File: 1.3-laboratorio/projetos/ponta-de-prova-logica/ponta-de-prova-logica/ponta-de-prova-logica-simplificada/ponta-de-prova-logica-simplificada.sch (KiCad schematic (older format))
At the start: 19 parts

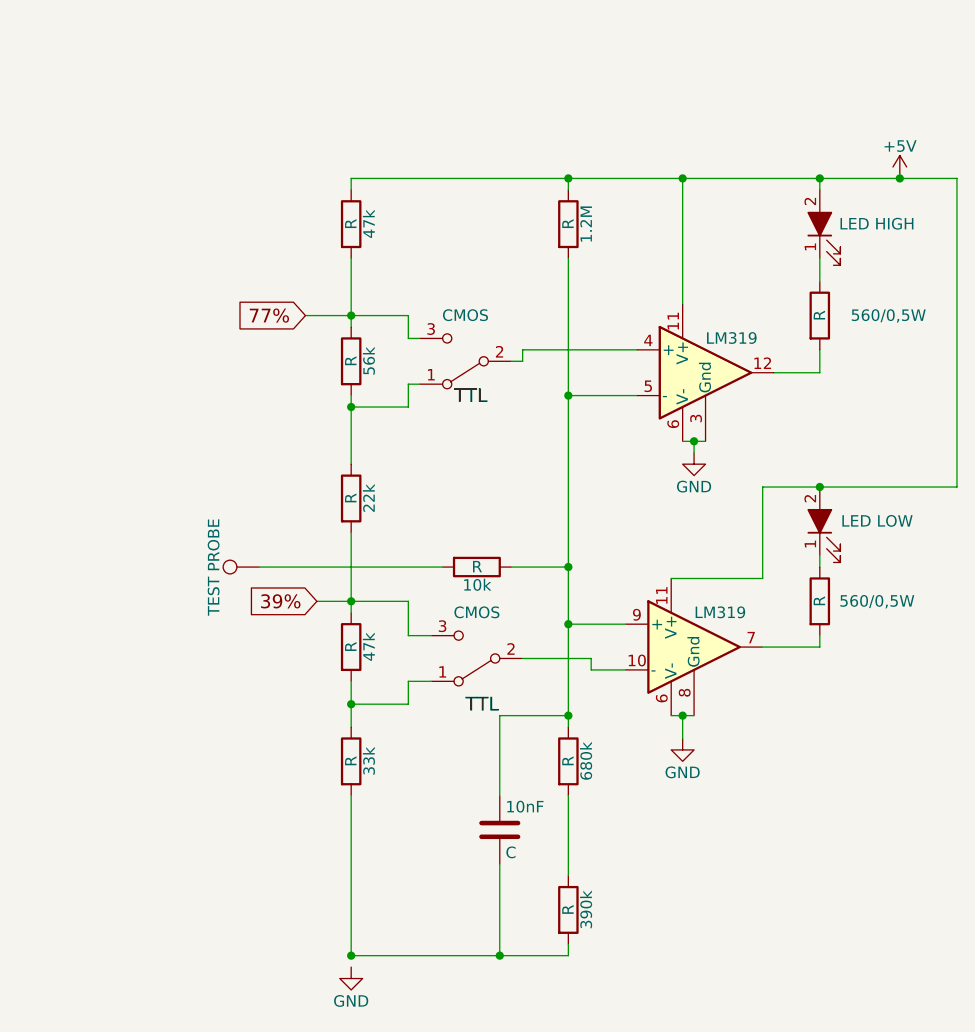
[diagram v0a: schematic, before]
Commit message: Desenho do Esquema PCB da ponta de prova lógica
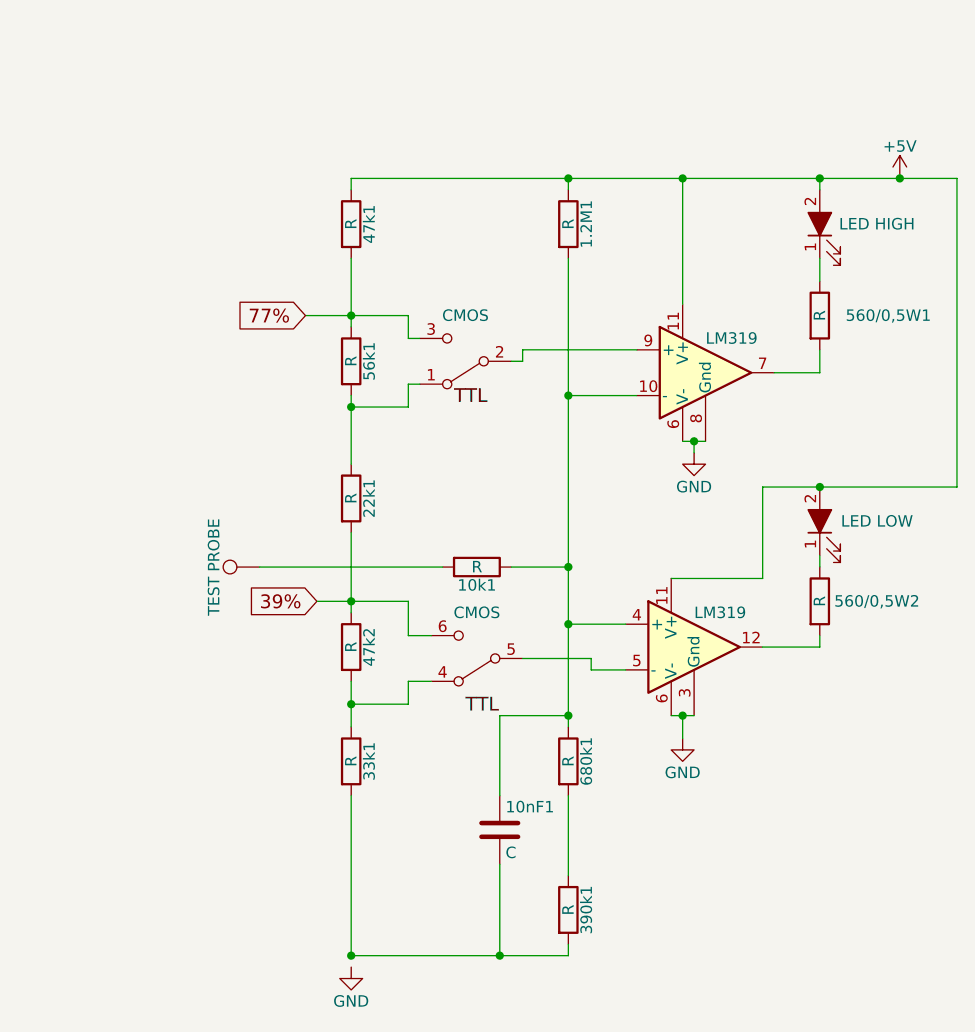
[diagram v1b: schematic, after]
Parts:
- 1.2M1: renamed from 1.2M; footprint (none) -> Resistors_THT:R_Axial_DIN0207_L6.3mm_D2.5mm_P7.62mm_Horizontal
- 10k1: renamed from 10k; footprint (none) -> Resistors_THT:R_Axial_DIN0207_L6.3mm_D2.5mm_P7.62mm_Horizontal
- 10nF1: renamed from 10nF; footprint (none) -> Capacitors_THT:C_Disc_D5.0mm_W2.5mm_P2.50mm
- 22k1: renamed from 22k; footprint (none) -> Resistors_THT:R_Axial_DIN0207_L6.3mm_D2.5mm_P7.62mm_Horizontal
- 33k1: renamed from 33k; footprint (none) -> Resistors_THT:R_Axial_DIN0207_L6.3mm_D2.5mm_P7.62mm_Horizontal
- 390k1: renamed from 390k; footprint (none) -> Resistors_THT:R_Axial_DIN0207_L6.3mm_D2.5mm_P7.62mm_Horizontal
- 47k1, 47k2: renamed from 47k; footprint (none) -> Resistors_THT:R_Axial_DIN0207_L6.3mm_D2.5mm_P7.62mm_Horizontal
- 560/0,5W1, 560/0,5W2: renamed from 560/0,5W; footprint (none) -> Resistors_THT:R_Axial_DIN0207_L6.3mm_D2.5mm_P7.62mm_Horizontal
- 56k1: renamed from 56k; footprint (none) -> Resistors_THT:R_Axial_DIN0207_L6.3mm_D2.5mm_P7.62mm_Horizontal
- 680k1: renamed from 680k; footprint (none) -> Resistors_THT:R_Axial_DIN0207_L6.3mm_D2.5mm_P7.62mm_Horizontal
- D1, D2: footprint (none) -> LEDs:LED_D1.8mm_W1.8mm_H2.4mm_Horizontal_O1.27mm_Z1.6mm
- J1: renamed from J?; footprint (none) -> Connectors:Pin_d1.0mm_L10.0mm
- TTL1: renamed from TTL; footprint (none) -> Buttons_Switches_THT:SW_CuK_JS202011AQN_DPDT_Angled
- U1: renamed from U?; footprint (none) -> Housings_DIP:DIP-14_W7.62mm
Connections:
- net 39%: now also TTL1.6 (C); no longer TTL1.3 (C)
- net GND: now also U1.3 (Gnd), U1.8 (Gnd); no longer U1.3 (Gnd), U1.8 (Gnd)
- net at 560/0,5W1.2: now also U1.7; no longer U1.12
- net at TTL1.2 (B): now also U1.9 (+); no longer U1.4 (+)
- net at 1.2M1.2, 10k1.1, 10nF1.1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: now also U1.10 (-), U1.4 (+); no longer U1.5 (-), U1.9 (+)
- net at 560/0,5W2.2: now also U1.12; no longer U1.7
- net at 33k1.1, 47k2.2: now also TTL1.4 (A); no longer TTL1.1 (A)
- new net: TTL1.5 (B), U1.5 (-)
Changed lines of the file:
@@
 LIBS:contrib
 LIBS:valves
+LIBS:ponta-de-prova-logica-simplificada-cache
 EELAYER 25 0
 EELAYER END
@@
 $EndDescr
 $Comp
-L LM319 U?
-U 1 1 5BBF01DE
+L LM319 U1
+U 2 1 5BBF01DE
 P 3850 2600
-F 0 "U?" H 3850 2850 50  0001 L CNN
+F 0 "U1" H 3850 2850 50  0001 L CNN
 F 1 "LM319" H 3850 2750 50  0000 L CNN
-F 2 "" H 3850 2600 50  0001 C CNN
+F 2 "Housings_DIP:DIP-14_W7.62mm" H 3850 2600 50  0001 C CNN
 F 3 "" H 3850 2600 50  0001 C CNN
-	1    3850 2600
-	1    0    0    -1
-$EndComp
-$Comp
-L +5V #PWR?
+	2    3850 2600
+	1    0    0    -1
+$EndComp
+$Comp
+L +5V #PWR01
 U 1 1 5BBF02C2
 P 4700 1750
-F 0 "#PWR?" H 4700 1600 50  0001 C CNN
+F 0 "#PWR01" H 4700 1600 50  0001 C CNN
 F 1 "+5V" H 4700 1890 50  0000 C CNN
 F 2 "" H 4700 1750 50  0001 C CNN
@@
 $EndComp
 $Comp
-L R 47k
+L R 47k2
 U 1 1 5BBF02DC
 P 2300 3800
-F 0 "47k" V 2380 3800 50  0000 C CNN
+F 0 "47k2" V 2380 3800 50  0000 C CNN
 F 1 "R" V 2300 3800 50  0000 C CNN
-F 2 "" V 2230 3800 50  0001 C CNN
+F 2 "Resistors_THT:R_Axial_DIN0207_L6.3mm_D2.5mm_P7.62mm_Horizontal" V 2230 3800 50  0001 C CNN
 F 3 "" H 2300 3800 50  0001 C CNN
 	1    2300 3800
@@
 $EndComp
 $Comp
-L R 33k
+L R 33k1
 U 1 1 5BBF0383
 P 2300 4300
-F 0 "33k" V 2380 4300 50  0000 C CNN
+F 0 "33k1" V 2380 4300 50  0000 C CNN
 F 1 "R" V 2300 4300 50  0000 C CNN
-F 2 "" V 2230 4300 50  0001 C CNN
+F 2 "Resistors_THT:R_Axial_DIN0207_L6.3mm_D2.5mm_P7.62mm_Horizontal" V 2230 4300 50  0001 C CNN
 F 3 "" H 2300 4300 50  0001 C CNN
 	1    2300 4300
@@
 $EndComp
 $Comp
-L R 56k
+L R 56k1
 U 1 1 5BBF0404
 P 2300 2550
-F 0 "56k" V 2380 2550 50  0000 C CNN
+F 0 "56k1" V 2380 2550 50  0000 C CNN
 F 1 "R" V 2300 2550 50  0000 C CNN
-F 2 "" V 2230 2550 50  0001 C CNN
+F 2 "Resistors_THT:R_Axial_DIN0207_L6.3mm_D2.5mm_P7.62mm_Horizontal" V 2230 2550 50  0001 C CNN
 F 3 "" H 2300 2550 50  0001 C CNN
 	1    2300 2550
@@
 $EndComp
 $Comp
-L R 22k
+L R 22k1
 U 1 1 5BBF043F
 P 2300 3150
-F 0 "22k" V 2380 3150 50  0000 C CNN
+F 0 "22k1" V 2380 3150 50  0000 C CNN
 F 1 "R" V 2300 3150 50  0000 C CNN
-F 2 "" V 2230 3150 50  0001 C CNN
+F 2 "Resistors_THT:R_Axial_DIN0207_L6.3mm_D2.5mm_P7.62mm_Horizontal" V 2230 3150 50  0001 C CNN
 F 3 "" H 2300 3150 50  0001 C CNN
 	1    2300 3150
@@
 $EndComp
 $Comp
-L R 390k
+L R 390k1
 U 1 1 5BBF0478
 P 3250 4950
-F 0 "390k" V 3330 4950 50  0000 C CNN
+F 0 "390k1" V 3330 4950 50  0000 C CNN
 F 1 "R" V 3250 4950 50  0000 C CNN
-F 2 "" V 3180 4950 50  0001 C CNN
+F 2 "Resistors_THT:R_Axial_DIN0207_L6.3mm_D2.5mm_P7.62mm_Horizontal" V 3180 4950 50  0001 C CNN
 F 3 "" H 3250 4950 50  0001 C CNN
 	1    3250 4950
@@
 $EndComp
 $Comp
-L R 680k
+L R 680k1
 U 1 1 5BBF04AF
 P 3250 4300
-F 0 "680k" V 3330 4300 50  0000 C CNN
+F 0 "680k1" V 3330 4300 50  0000 C CNN
 F 1 "R" V 3250 4300 50  0000 C CNN
-F 2 "" V 3180 4300 50  0001 C CNN
+F 2 "Resistors_THT:R_Axial_DIN0207_L6.3mm_D2.5mm_P7.62mm_Horizontal" V 3180 4300 50  0001 C CNN
 F 3 "" H 3250 4300 50  0001 C CNN
 	1    3250 4300
@@
 $EndComp
 $Comp
-L R 47k
+L R 47k1
 U 1 1 5BBF0ACE
 P 2300 1950
-F 0 "47k" V 2380 1950 50  0000 C CNN
+F 0 "47k1" V 2380 1950 50  0000 C CNN
 F 1 "R" V 2300 1950 50  0000 C CNN
-F 2 "" V 2230 1950 50  0001 C CNN
+F 2 "Resistors_THT:R_Axial_DIN0207_L6.3mm_D2.5mm_P7.62mm_Horizontal" V 2230 1950 50  0001 C CNN
 F 3 "" H 2300 1950 50  0001 C CNN
 	1    2300 1950
@@
 $EndComp
 $Comp
-L R 1.2M
+L R 1.2M1
 U 1 1 5BBF0B71
 P 3250 1950
-F 0 "1.2M" V 3330 1950 50  0000 C CNN
+F 0 "1.2M1" V 3330 1950 50  0000 C CNN
 F 1 "R" V 3250 1950 50  0000 C CNN
-F 2 "" V 3180 1950 50  0001 C CNN
+F 2 "Resistors_THT:R_Axial_DIN0207_L6.3mm_D2.5mm_P7.62mm_Horizontal" V 3180 1950 50  0001 C CNN
 F 3 "" H 3250 1950 50  0001 C CNN
 	1    3250 1950
@@
 $EndComp
 $Comp
-L R 560/0,5W
+L R 560/0,5W1
 U 1 1 5BBF0C0A
 P 4350 2350
-F 0 "560/0,5W" H 4650 2350 50  0000 C CNN
+F 0 "560/0,5W1" H 4650 2350 50  0000 C CNN
 F 1 "R" V 4350 2350 50  0000 C CNN
-F 2 "" V 4280 2350 50  0001 C CNN
+F 2 "Resistors_THT:R_Axial_DIN0207_L6.3mm_D2.5mm_P7.62mm_Horizontal" V 4280 2350 50  0001 C CNN
 F 3 "" H 4350 2350 50  0001 C CNN
 	1    4350 2350
@@
 $EndComp
 $Comp
-L R 10k
+L R 10k1
 U 1 1 5BBF0C7D
 P 2850 3450
-F 0 "10k" V 2930 3450 50  0000 C CNN
+F 0 "10k1" V 2930 3450 50  0000 C CNN
 F 1 "R" V 2850 3450 50  0000 C CNN
-F 2 "" V 2780 3450 50  0001 C CNN
+F 2 "Resistors_THT:R_Axial_DIN0207_L6.3mm_D2.5mm_P7.62mm_Horizontal" V 2780 3450 50  0001 C CNN
 F 3 "" H 2850 3450 50  0001 C CNN
 	1    2850 3450
@@
 F 0 "D1" H 4350 2050 50  0001 C CNN
 F 1 "LED HIGH" V 4350 1700 50  0000 C CNN
-F 2 "" H 4350 1950 50  0001 C CNN
+F 2 "LEDs:LED_D1.8mm_W1.8mm_H2.4mm_Horizontal_O1.27mm_Z1.6mm" H 4350 1950 50  0001 C CNN
 F 3 "" H 4350 1950 50  0001 C CNN
 	1    4350 1950
@@
 F 0 "D2" H 4350 3350 50  0001 C CNN
 F 1 "LED LOW" V 4350 3000 50  0000 C CNN
-F 2 "" H 4350 3250 50  0001 C CNN
+F 2 "LEDs:LED_D1.8mm_W1.8mm_H2.4mm_Horizontal_O1.27mm_Z1.6mm" H 4350 3250 50  0001 C CNN
 F 3 "" H 4350 3250 50  0001 C CNN
 	1    4350 3250
@@
 $EndComp
 $Comp
-L TEST_1P J?
+L TEST_1P J1
 U 1 1 5BBF1BCB
 P 1900 3450
-F 0 "J?" H 1900 3720 50  0001 C CNN
+F 0 "J1" H 1900 3720 50  0001 C CNN
 F 1 "TEST PROBE" H 1900 3650 50  0000 C CNN
-F 2 "" H 2100 3450 50  0001 C CNN
+F 2 "Connectors:Pin_d1.0mm_L10.0mm" H 2100 3450 50  0001 C CNN
 F 3 "" H 2100 3450 50  0001 C CNN
 	1    1900 3450
@@
 $EndComp
 $Comp
-L GND #PWR?
+L GND #PWR02
 U 1 1 5BBF1EC9
 P 2300 5200
-F 0 "#PWR?" H 2300 4950 50  0001 C CNN
+F 0 "#PWR02" H 2300 4950 50  0001 C CNN
 F 1 "GND" H 2300 5050 50  0000 C CNN
 F 2 "" H 2300 5200 50  0001 C CNN
@@
 $EndComp
 $Comp
-L R 560/0,5W
+L R 560/0,5W2
 U 1 1 5BBF372D
 P 4350 3600
-F 0 "560/0,5W" H 4600 3600 50  0000 C CNN
+F 0 "560/0,5W2" H 4600 3600 50  0000 C CNN
 F 1 "R" V 4350 3600 50  0000 C CNN
-F 2 "" V 4280 3600 50  0001 C CNN
+F 2 "Resistors_THT:R_Axial_DIN0207_L6.3mm_D2.5mm_P7.62mm_Horizontal" V 4280 3600 50  0001 C CNN
 F 3 "" H 4350 3600 50  0001 C CNN
 	1    4350 3600
@@
 $EndComp
 $Comp
-L GND #PWR?
+L GND #PWR03
 U 1 1 5BBF3B02
 P 3800 2950
-F 0 "#PWR?" H 3800 2700 50  0001 C CNN
+F 0 "#PWR03" H 3800 2700 50  0001 C CNN
 F 1 "GND" H 3800 2800 50  0000 C CNN
 F 2 "" H 3800 2950 50  0001 C CNN
@@
 $EndComp
 $Comp
-L GND #PWR?
+L GND #PWR04
 U 1 1 5BBF3BC6
 P 3750 4200
-F 0 "#PWR?" H 3750 3950 50  0001 C CNN
+F 0 "#PWR04" H 3750 3950 50  0001 C CNN
 F 1 "GND" H 3750 4050 50  0000 C CNN
 F 2 "" H 3750 4200 50  0001 C CNN
@@
 Connection ~ 4350 1750
 $Comp
-L SW_DPDT_x2 TTL
-U 1 1 5BBF4AF5
+L SW_DPDT_x2 TTL1
+U 2 1 5BBF4AF5
 P 2850 3850
-F 0 "TTL" H 2850 4020 50  0001 C CNN
+F 0 "TTL1" H 2850 4020 50  0001 C CNN
 F 1 "CMOS" H 2850 3650 50  0000 C CNN
-F 2 "" H 2850 3850 50  0001 C CNN
+F 2 "Buttons_Switches_THT:SW_CuK_JS202011AQN_DPDT_Angled" H 2850 3850 50  0001 C CNN
 F 3 "" H 2850 3850 50  0001 C CNN
-	1    2850 3850
+	2    2850 3850
 	-1   0    0    1
 $EndComp
@@
 Connection ~ 2300 4050
 $Comp
-L SW_DPDT_x2 TTL
+L SW_DPDT_x2 TTL1
 U 1 1 5BBF503E
 P 2800 2550
-F 0 "TTL" H 2800 2720 50  0001 C CNN
+F 0 "TTL1" H 2800 2720 50  0001 C CNN
 F 1 "CMOS" H 2800 2350 50  0000 C CNN
-F 2 "" H 2800 2550 50  0001 C CNN
+F 2 "Buttons_Switches_THT:SW_CuK_JS202011AQN_DPDT_Angled" H 2800 2550 50  0001 C CNN
 F 3 "" H 2800 2550 50  0001 C CNN
 	1    2800 2550
@@
 	4350 3800 4100 3800
 $Comp
-L LM319 U?
-U 2 1 5BBF0257
+L LM319 U1
+U 1 1 5BBF0257
 P 3800 3800
-F 0 "U?" H 3800 4050 50  0001 L CNN
+F 0 "U1" H 3800 4050 50  0001 L CNN
 F 1 "LM319" H 3800 3950 50  0000 L CNN
-F 2 "" H 3800 3800 50  0001 C CNN
+F 2 "Housings_DIP:DIP-14_W7.62mm" H 3800 3800 50  0001 C CNN
 F 3 "" H 3800 3800 50  0001 C CNN
-	2    3800 3800
+	1    3800 3800
 	1    0    0    -1
 $EndComp
@@
 77%
 $Comp
-L C 10nF
+L C 10nF1
 U 1 1 5BBF9380
 P 2950 4600
-F 0 "10nF" H 2975 4700 50  0000 L CNN
+F 0 "10nF1" H 2975 4700 50  0000 L CNN
 F 1 "C" H 2975 4500 50  0000 L CNN
-F 2 "" H 2988 4450 50  0001 C CNN
+F 2 "Capacitors_THT:C_Disc_D5.0mm_W2.5mm_P2.50mm" H 2988 4450 50  0001 C CNN
 F 3 "" H 2950 4600 50  0001 C CNN
 	1    2950 4600

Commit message: Alterações no esquemático da ponta de prova simplificada
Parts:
- added J?: Conn_01x02, symbol Conn_01x02
- C1: renamed from 10nF1; value C -> 10nF
- R1: renamed from 47k1; value R -> 47k
- R10: renamed from 680k1; value R -> 680k
- R11: renamed from 390k1; value R -> 390k
- R2: renamed from 1.2M1; value R -> 1.2M
- R3: renamed from 560/0,5W1; value R -> 560/0.5W
- R4: renamed from 56k1; value R -> 56k
- R5: renamed from 22k1; value R -> 22k
- R6: renamed from 10k1; value R -> 10k
- R7: renamed from 560/0,5W2; value R -> 560/0.5W
- R8: renamed from 47k2; value R -> 47k
- R9: renamed from 33k1; value R -> 33k
- TTL1: value CMOS -> SW_DPDT_x2
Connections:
- net +5V: now also J?.2 (Pin_2)
- net 39%: no longer R5.2, R8.1, TTL1.6 (C)
- net 77%: no longer R1.2, R4.1, TTL1.3 (C)
- net GND: now also C1.2, R11.2, R9.2, J?.1 (Pin_1)
- new net: R5.2, R8.1, TTL1.6 (C)
- new net: R1.2, R4.1, TTL1.3 (C)
